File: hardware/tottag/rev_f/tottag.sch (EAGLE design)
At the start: 145 parts, among them J1 MICRO_USB_B_HIROSE_ZX62-B-5PA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, J2 CON_MICRO_SDDM3AT-SF-PEJM5, J3 BAT_HOLE, J4 TC2030-JLINK-NL, J5 TC2030-JLINK-NL, T1 HHM1595A1, U1 DW1000, U10 STM32F091CC, U2 FT232RQ, U3 LIS2DW12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

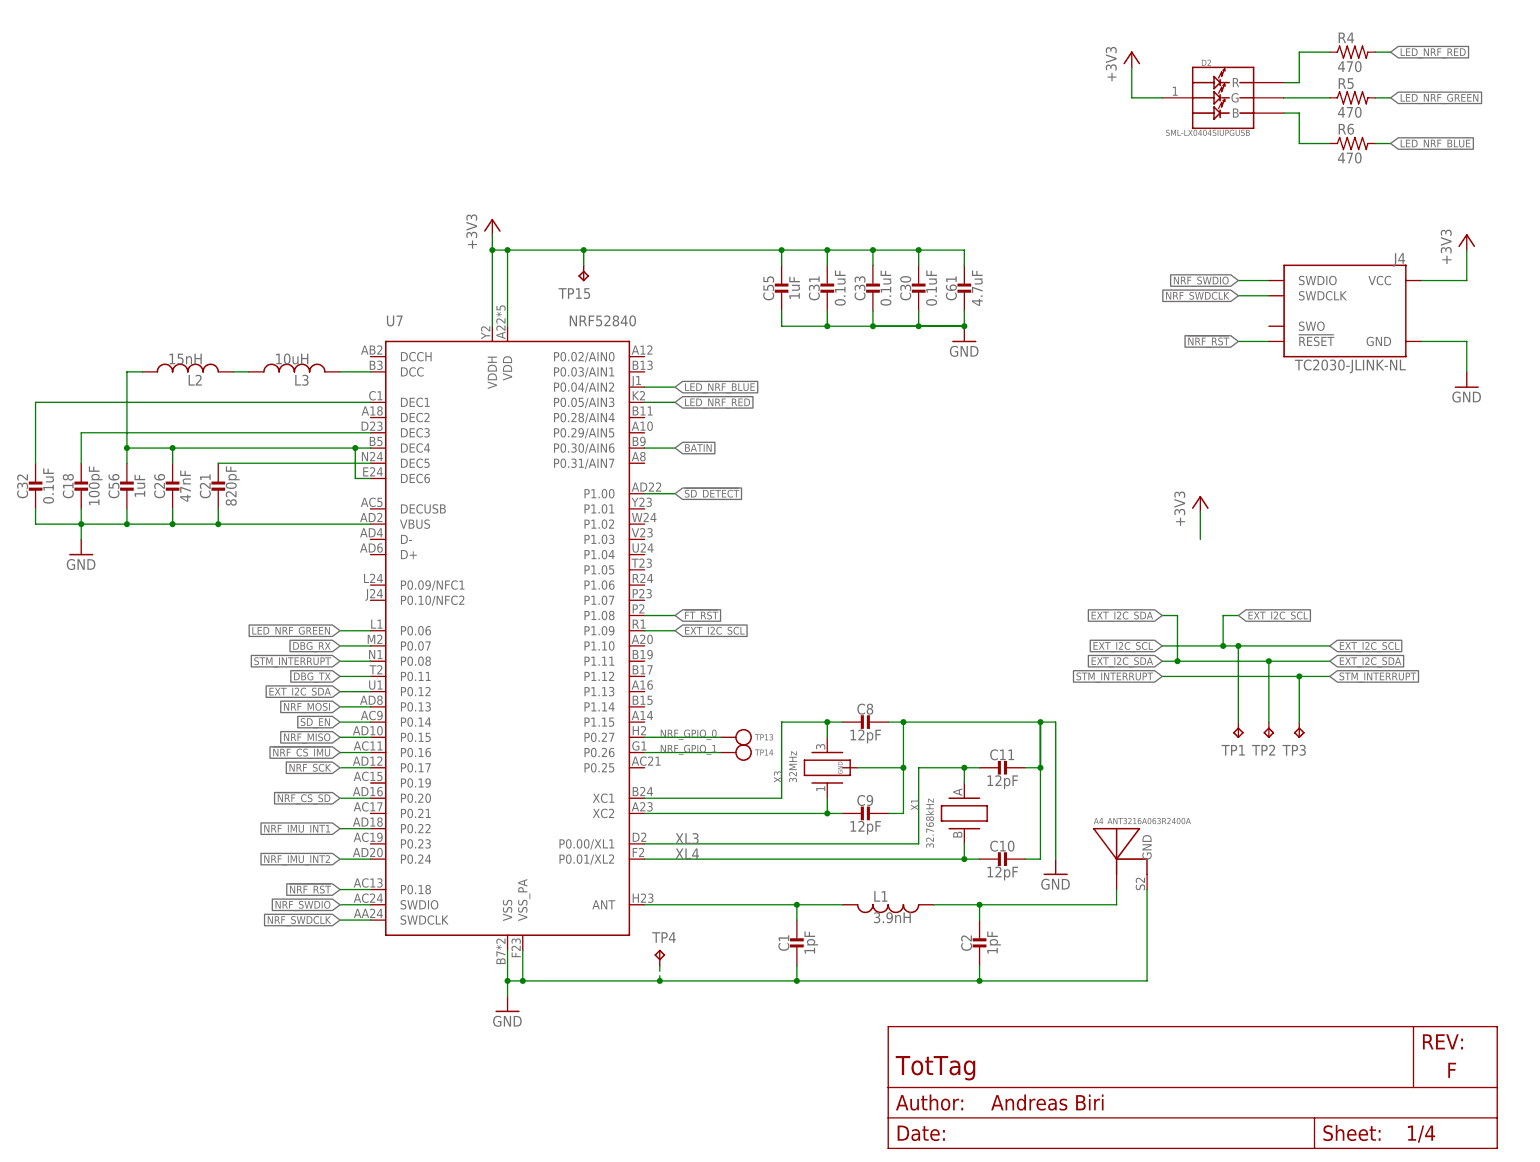
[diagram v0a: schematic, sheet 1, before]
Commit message: added RTC to schematic; supply battery still missing
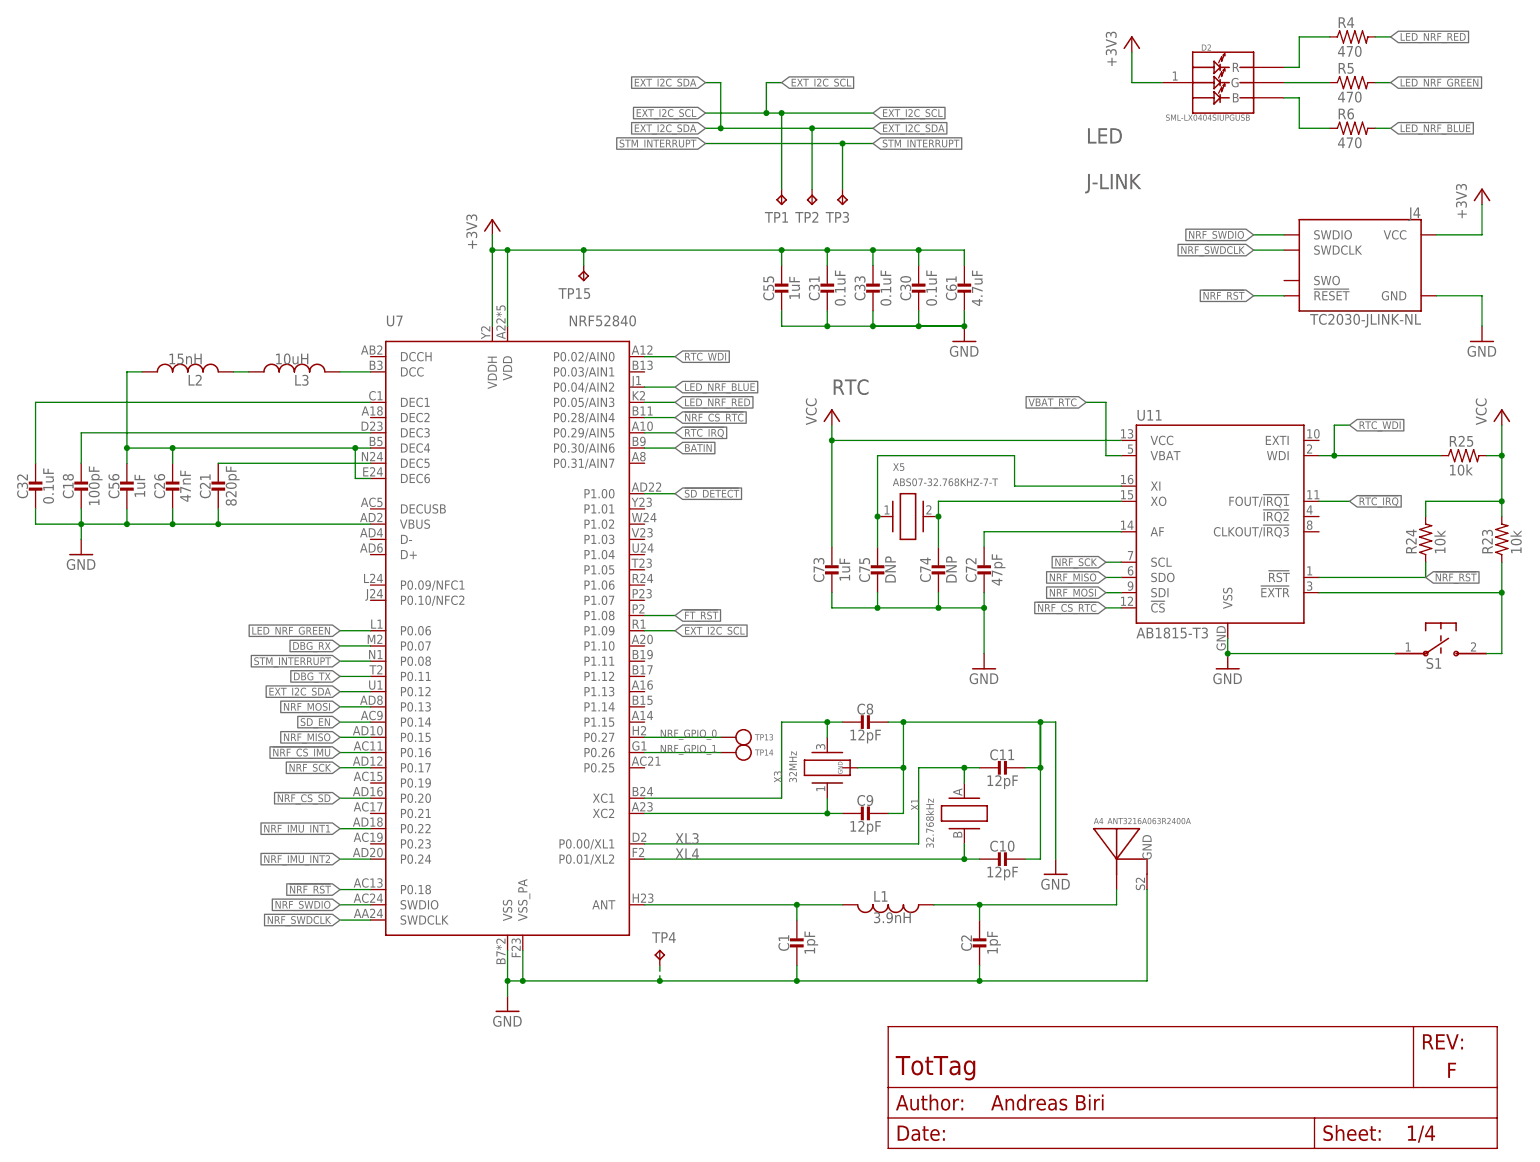
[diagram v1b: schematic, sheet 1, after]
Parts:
- added C72: 47pF, passives:CAPACITOR0402_CAP
- added C73: 1uF, passives:CAPACITOR0402_CAP
- added C74, C75: DNP, passives:CAPACITOR0402_CAP
- added R23, R24, R25: 10k, passives:RESISTOR0402_RES
- added S1: B3U-1000P, switches:B3U-1000P
- added U11: AB1815-T3, chips:AB1815-T3
- added X5: ABS07-32.768KHZ-7-T, crystals:ABS07-32.768KHZ-7-T
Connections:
- new net !NRF_CS_RTC: U11.!CS, U7.P0.28/AIN4
- new net !RTC_EXTR: R23.1, S1.P$2, U11.!EXTR
- new net !RTC_IRQ: U11.FOUT/!IRQ1, U7.P0.29/AIN5
- new net N$35: C72.1, U11.AF
- new net N$41: C75.1, U11.XI, X5.1
- new net N$42: C74.1, U11.XO, X5.2
- new net RTC_WDI: R25.1, U11.WDI, U7.P0.02/AIN0
- new net VBAT_RTC: U11.VBAT
- new net VCC: C73.1, R23.2, R24.2, R25.2, U11.VCC
- net !NRF_RST: now also R24.1, U11.!RST
- net GND: now also C72.2, C73.2, C74.2, C75.2, S1.P$1, U11.VSS
- net NRF_MISO: now also U11.SDO
- net NRF_MOSI: now also U11.SDI
- net NRF_SCK: now also U11.SCL
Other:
- note added: "J-LINK"
- note added: "RTC"
- moved on the sheet: D2, J4, R4, R5, R6, TP1, TP2, TP3

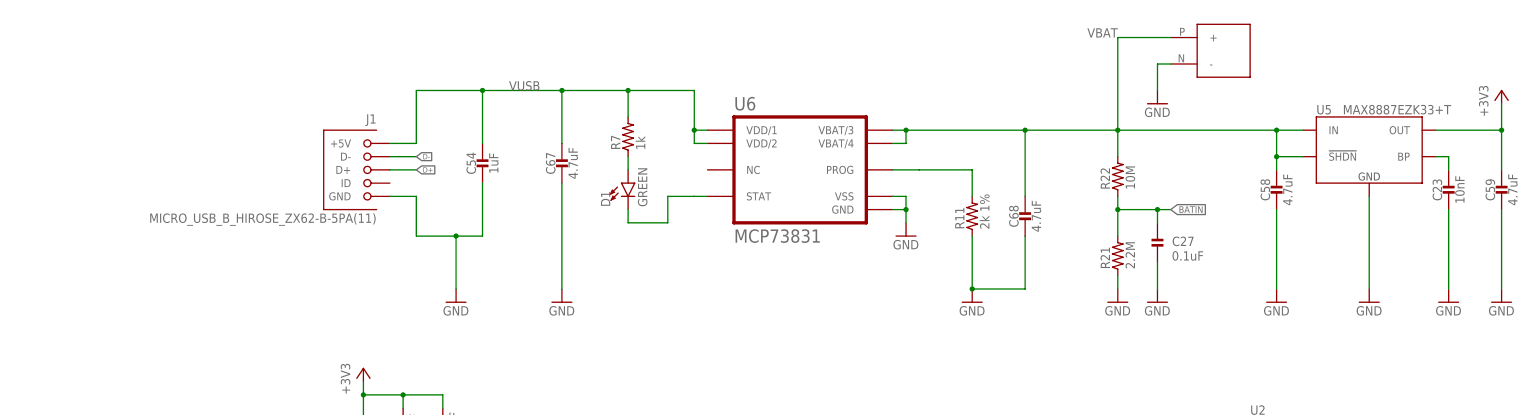
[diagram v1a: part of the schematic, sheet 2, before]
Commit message: added battery, fixed RTC passives
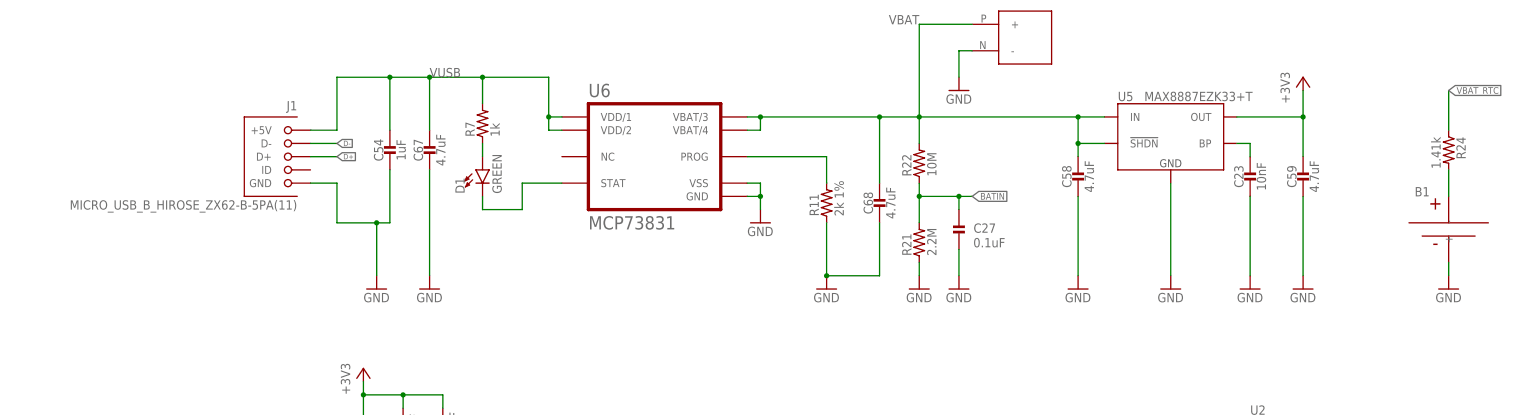
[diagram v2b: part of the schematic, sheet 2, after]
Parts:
- removed C74, C75: DNP, passives:CAPACITOR0402_CAP
- removed S1: B3U-1000P, switches:B3U-1000P
- added B1: (no value), batteries:MS518SE
- R24: value 10k -> 1.41k
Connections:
- removed net !RTC_EXTR: R23.1, S1.P$2, U11.!EXTR
- new net N$43: R23.1, U11.EXTI
- new net N$45: B1.+, R24.2
- net !NRF_RST: no longer R24.1, U11.!RST
- net GND: now also B1.-, U11.!EXTR; no longer C74.2, C75.2, S1.P$1
- net N$41: no longer C75.1
- net N$42: no longer C74.1
- net VBAT_RTC: now also R23.2, R24.1, R25.2
- net VCC: no longer R23.2, R24.2, R25.2
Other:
- note added: "90 Ohm"
- note added: "Backup Battery for RTC"
- note added: "Be aware that the DecaWave is very sensitive regarding its power supply. We suggest using the "MAX8887EZK33+T" from Maxim Integrated. You can find a reference layout at github.com/lab11/totternary/hardware/tottag."
- note added: "VBAT ESR must be 1.5kOhm for optimal performance"
- note removed: "Be aware that the DecaWave is very sensitive regarding its power supply. We suggest using the "MAX8887EZK33+T" from Maxim Integrated. You can find a reference layout at github.com/lab11/polypoint/pcb/tritag."
- moved on the sheet: C23, C27, C54, C58, C59, C67, C68, C73, D1, J1, R11, R21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

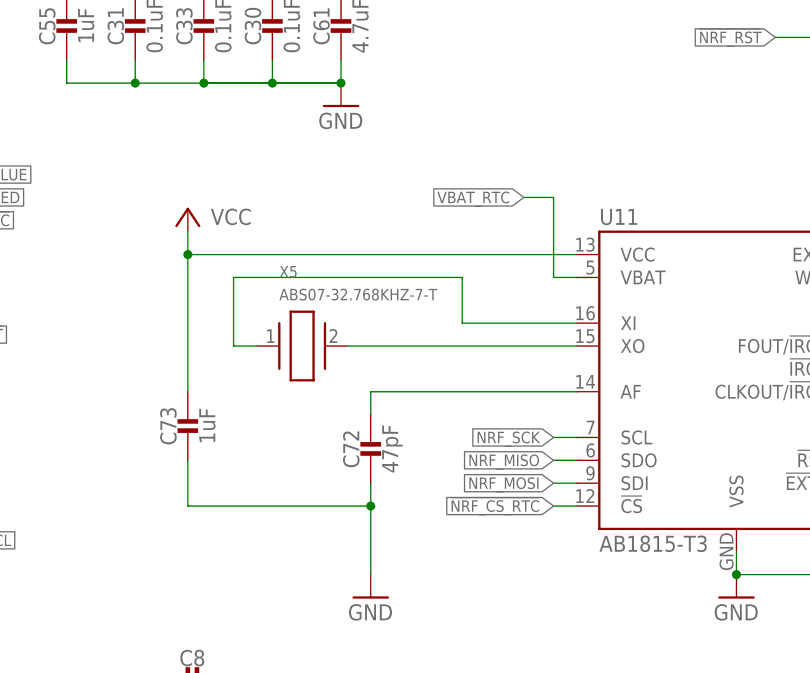
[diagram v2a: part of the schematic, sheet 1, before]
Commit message: add pull-up for CS to prevent floating if nRF is turned off
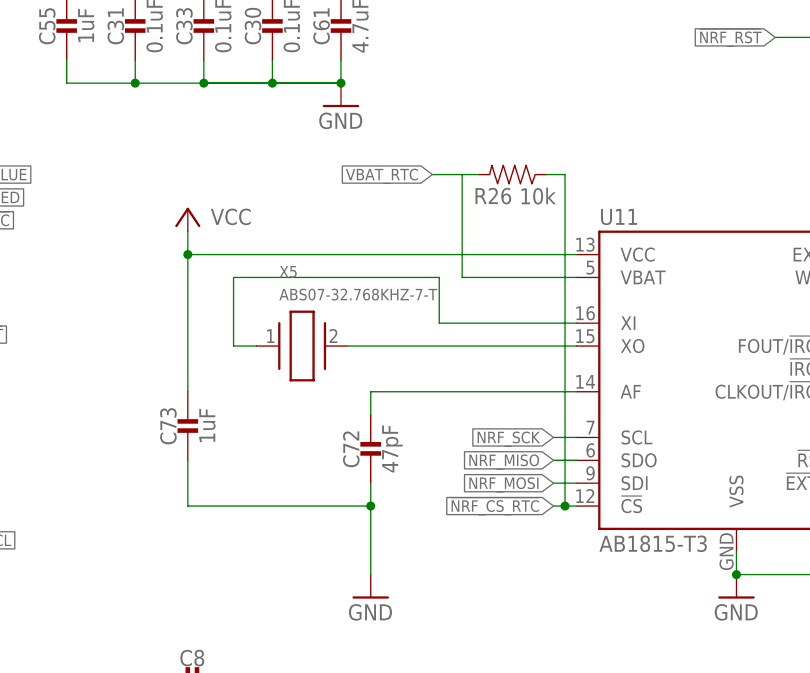
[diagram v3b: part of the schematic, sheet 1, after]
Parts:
- added R26: 10k, passives:RESISTOR0402_RES
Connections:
- net !NRF_CS_RTC: now also R26.1
- net VBAT_RTC: now also R26.2
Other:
- note added: "Pull-up nCS to prevent float"
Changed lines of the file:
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@@
+<attribute name="MPN" value="RC0402JR-0710KL"/>
+</part>
+<part name="R26" library="passives" deviceset="RESISTOR" device="0402_RES" value="10k">
+<attribute name="DIGIKEY" value="311-10KJRCT-ND "/>
 <attribute name="MPN" value="RC0402JR-0710KL"/>
 </part>
@@
 <text x="180.34" y="160.02" size="2.54" layer="98">J-LINK</text>
 <text x="180.34" y="167.64" size="2.54" layer="98">LED</text>
+<text x="188.722" y="126.238" size="1.778" layer="98">Pull-up nCS to prevent float</text>
 </plain>
 <instances>
@@
 <instance part="P+16" gate="VCC" x="143.002" y="123.19" smashed="yes">
 <attribute name="VALUE" x="145.542" y="121.412" size="1.778" layer="96"/>
+</instance>
+<instance part="R26" gate="G$1" x="177.8" y="127" smashed="yes" rot="R180">
+<attribute name="DIGIKEY" x="177.8" y="127" size="1.778" layer="96" rot="R180" display="off"/>
+<attribute name="MPN" x="177.8" y="127" size="1.778" layer="96" rot="R180" display="off"/>
+<attribute name="NAME" x="179.07" y="125.5014" size="1.778" layer="95" rot="R180"/>
+<attribute name="VALUE" x="183.896" y="125.476" size="1.778" layer="96" rot="R180"/>
 </instance>
 </instances>
@@
 <net name="N$41" class="0">
 <segment>
-<wire x1="148.082" y1="115.57" x2="173.482" y2="115.57" width="0.1524" layer="91"/>
-<wire x1="173.482" y1="115.57" x2="173.482" y2="110.49" width="0.1524" layer="91"/>
+<wire x1="148.082" y1="115.57" x2="170.942" y2="115.57" width="0.1524" layer="91"/>
+<wire x1="170.942" y1="115.57" x2="170.942" y2="110.49" width="0.1524" layer="91"/>
 <pinref part="U11" gate="G$1" pin="XI"/>
-<wire x1="173.482" y1="110.49" x2="186.182" y2="110.49" width="0.1524" layer="91"/>
+<wire x1="170.942" y1="110.49" x2="186.182" y2="110.49" width="0.1524" layer="91"/>
 <pinref part="X5" gate="G$1" pin="1"/>
 <wire x1="148.082" y1="115.57" x2="148.082" y2="107.95" width="0.1524" layer="91"/>
@@
 <segment>
 <pinref part="U11" gate="G$1" pin="!CS"/>
-<wire x1="186.182" y1="90.17" x2="183.642" y2="90.17" width="0.1524" layer="91"/>
+<wire x1="186.182" y1="90.17" x2="184.912" y2="90.17" width="0.1524" layer="91"/>
 <label x="183.642" y="90.17" size="1.27" layer="95" rot="R180" xref="yes"/>
+<pinref part="R26" gate="G$1" pin="1"/>
+<wire x1="184.912" y1="90.17" x2="183.642" y2="90.17" width="0.1524" layer="91"/>
+<wire x1="182.88" y1="127" x2="184.912" y2="127" width="0.1524" layer="91"/>
+<wire x1="184.912" y1="127" x2="184.912" y2="90.17" width="0.1524" layer="91"/>
+<junction x="184.912" y="90.17"/>
 </segment>
 <segment>
@@
 <segment>
 <pinref part="U11" gate="G$1" pin="VBAT"/>
-<wire x1="186.182" y1="115.57" x2="183.642" y2="115.57" width="0.1524" layer="91"/>
-<wire x1="183.642" y1="115.57" x2="183.642" y2="124.46" width="0.1524" layer="91"/>
-<label x="180.34" y="124.46" size="1.27" layer="95" rot="R180" xref="yes"/>
-<wire x1="180.34" y1="124.46" x2="183.642" y2="124.46" width="0.1524" layer="91"/>
-</segment>
-<segment>
+<wire x1="186.182" y1="115.57" x2="173.482" y2="115.57" width="0.1524" layer="91"/>
+<wire x1="173.482" y1="115.57" x2="173.482" y2="127" width="0.1524" layer="91"/>
+<label x="170.18" y="127" size="1.27" layer="95" rot="R180" xref="yes"/>
+<wire x1="170.18" y1="127" x2="172.72" y2="127" width="0.1524" layer="91"/>
+<pinref part="R26" gate="G$1" pin="2"/>
+<wire x1="172.72" y1="127" x2="173.482" y2="127" width="0.1524" layer="91"/>
+<wire x1="175.26" y1="127" x2="173.482" y2="127" width="0.1524" layer="91"/>
+</segment>
+<segment>

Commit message: routing finished; hardware revision F ready for review
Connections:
- net !NRF_CS_RTC: now also U7.P0.29/AIN5; no longer U7.P0.28/AIN4
- net !RTC_IRQ: now also U7.P0.02/AIN0; no longer U7.P0.29/AIN5
- net RTC_WDI: now also U7.P0.31/AIN7; no longer U7.P0.02/AIN0
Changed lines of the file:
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@@
 </segment>
 <segment>
-<pinref part="U7" gate="G$1" pin="P0.29/AIN5"/>
-<wire x1="106.68" y1="119.38" x2="111.76" y2="119.38" width="0.1524" layer="91"/>
-<label x="111.76" y="119.38" size="1.27" layer="95" xref="yes"/>
+<pinref part="U7" gate="G$1" pin="P0.02/AIN0"/>
+<wire x1="106.68" y1="132.08" x2="111.76" y2="132.08" width="0.1524" layer="91"/>
+<label x="111.76" y="132.08" size="1.27" layer="95" xref="yes"/>
 </segment>
 </net>
@@
 </segment>
 <segment>
-<pinref part="U7" gate="G$1" pin="P0.02/AIN0"/>
-<wire x1="106.68" y1="132.08" x2="111.76" y2="132.08" width="0.1524" layer="91"/>
-<label x="111.76" y="132.08" size="1.27" layer="95" xref="yes"/>
+<pinref part="U7" gate="G$1" pin="P0.31/AIN7"/>
+<wire x1="106.68" y1="114.3" x2="111.76" y2="114.3" width="0.1524" layer="91"/>
+<label x="111.76" y="114.3" size="1.27" layer="95" xref="yes"/>
 </segment>
 </net>
@@
 </segment>
 <segment>
-<pinref part="U7" gate="G$1" pin="P0.28/AIN4"/>
-<wire x1="106.68" y1="121.92" x2="111.76" y2="121.92" width="0.1524" layer="91"/>
-<label x="111.76" y="121.92" size="1.27" layer="95" xref="yes"/>
+<pinref part="U7" gate="G$1" pin="P0.29/AIN5"/>
+<wire x1="106.68" y1="119.38" x2="111.76" y2="119.38" width="0.1524" layer="91"/>
+<label x="111.76" y="119.38" size="1.27" layer="95" xref="yes"/>
 </segment>
 </net>
@@
 <wire x1="173.482" y1="115.57" x2="173.482" y2="127" width="0.1524" layer="91"/>
 <label x="170.18" y="127" size="1.27" layer="95" rot="R180" xref="yes"/>
-<wire x1="170.18" y1="127" x2="172.72" y2="127" width="0.1524" layer="91"/>
+<wire x1="170.18" y1="127" x2="173.482" y2="127" width="0.1524" layer="91"/>
 <pinref part="R26" gate="G$1" pin="2"/>
-<wire x1="172.72" y1="127" x2="173.482" y2="127" width="0.1524" layer="91"/>
 <wire x1="175.26" y1="127" x2="173.482" y2="127" width="0.1524" layer="91"/>
+<junction x="173.482" y="127"/>
 </segment>
 <segment>
